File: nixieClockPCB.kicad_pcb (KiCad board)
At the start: 2 copper layers, 51 x 30.3 mm, 23 parts, among them M1 1364_HV, U1 74141, U10 WeMos_D1_mini, U2 74141, U3 74141, U4 74141, U5 74141, U6 74141, U7 74AHC595, U8 74AHC595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

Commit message: layout moving.
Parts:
- removed the M1 at (42.0, 90.5)
- added M2: Nch8200hv, Nixie_footprint_lib:Nch8200hv, B.Cu at (189.2, 27.4)
- M1: renamed from U10; moved to B.Cu
- U1, U2, U3, U4, U5, U6: footprint Package_DIP:DIP-16_W7.62mm_LongPads -> Package_DIP:DIP-16_W7.62mm
- U7, U8, U9: footprint Package_DIP:DIP-16_W7.62mm_LongPads -> nixiemisc:nixiemisc-SOIC16-5.3MM; moved to B.Cu
- moved R1 115.9 mm to (18.6, 32.6), turned to -90 degrees
- moved M1 109.1 mm to (149.1, 65.4), turned to 180 degrees
- moved U6 106.7 mm to (161.8, 19.5), turned to -90 degrees
- moved N1 101.5 mm to (27.4, 32.8), turned to 180 degrees
- moved N6 83.4 mm to (152.9, 32.8), turned to 180 degrees
- moved R2 78.5 mm to (40.1, 32.6), turned to -90 degrees
- moved N2 76.7 mm to (48.9, 32.8), turned to 180 degrees
- moved U5 74.6 mm to (139.6, 19.5), turned to -90 degrees
- moved U1 70.4 mm to (36.3, 19.5), turned to -90 degrees
- moved N3 60.8 mm to (78.9, 32.8), turned to 180 degrees
- moved R5 57.3 mm to (121.9, 32.6), turned to -90 degrees
- moved N5 52.3 mm to (130.7, 32.8), turned to 180 degrees
- moved R3 48.1 mm to (70.1, 32.6), turned to -90 degrees
- moved U2 47.6 mm to (57.8, 19.5), turned to -90 degrees
- moved N4 40.6 mm to (101.9, 32.8), turned to 180 degrees
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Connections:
- U1 pad 3: unconnected-(U1-Pad3) -> N1_A
- U1 pad 4: unconnected-(U1-Pad4) -> N1_D
- U1 pad 6: unconnected-(U1-Pad6) -> N1_B
- U1 pad 7: unconnected-(U1-Pad7) -> N1_C
- U2 pad 3: unconnected-(U2-Pad3) -> N2_A
- U2 pad 4: unconnected-(U2-Pad4) -> N2_D
- U2 pad 6: unconnected-(U2-Pad6) -> N2_B
- U2 pad 7: unconnected-(U2-Pad7) -> N2_C
- U3 pad 3: unconnected-(U3-Pad3) -> N3_A
- U3 pad 4: unconnected-(U3-Pad4) -> N3_D
- U3 pad 6: unconnected-(U3-Pad6) -> N3_B
- U3 pad 7: unconnected-(U3-Pad7) -> N3_C
- U4 pad 3: unconnected-(U4-Pad3) -> N4_A
- U4 pad 4: unconnected-(U4-Pad4) -> N4_D
- U4 pad 6: unconnected-(U4-Pad6) -> N4_B
- U4 pad 7: unconnected-(U4-Pad7) -> N4_C
- U5 pad 3: unconnected-(U5-Pad3) -> N5_A
- U5 pad 4: unconnected-(U5-Pad4) -> N5_D
- U5 pad 6: unconnected-(U5-Pad6) -> N5_B
- U5 pad 7: unconnected-(U5-Pad7) -> N5_C
- U6 pad 3: unconnected-(U6-Pad3) -> N6_A
- U6 pad 4: unconnected-(U6-Pad4) -> N6_D
- U6 pad 6: unconnected-(U6-Pad6) -> N6_B
- U6 pad 7: unconnected-(U6-Pad7) -> N6_C
- U7 pad 1: unconnected-(U7-Pad1) -> N1_B
- U7 pad 15: unconnected-(U7-Pad15) -> N1_A
- U7 pad 2: unconnected-(U7-Pad2) -> N1_C
- U7 pad 3: unconnected-(U7-Pad3) -> N1_D
- U7 pad 4: unconnected-(U7-Pad4) -> N2_A
- U7 pad 5: unconnected-(U7-Pad5) -> N2_B
- U7 pad 6: unconnected-(U7-Pad6) -> N2_C
- U7 pad 7: unconnected-(U7-Pad7) -> N2_D
- U8 pad 1: unconnected-(U8-Pad1) -> N3_B
- U8 pad 15: unconnected-(U8-Pad15) -> N3_A
- U8 pad 2: unconnected-(U8-Pad2) -> N3_C
- U8 pad 3: unconnected-(U8-Pad3) -> N3_D
- U8 pad 4: unconnected-(U8-Pad4) -> N4_A
- U8 pad 5: unconnected-(U8-Pad5) -> N4_B
- U8 pad 6: unconnected-(U8-Pad6) -> N4_C
- U8 pad 7: unconnected-(U8-Pad7) -> N4_D
- U9 pad 1: unconnected-(U9-Pad1) -> N5_B
- U9 pad 15: unconnected-(U9-Pad15) -> N5_A
- U9 pad 2: unconnected-(U9-Pad2) -> N5_C
- U9 pad 3: unconnected-(U9-Pad3) -> N5_D
- U9 pad 4: unconnected-(U9-Pad4) -> N6_A
- U9 pad 5: unconnected-(U9-Pad5) -> N6_B
- U9 pad 6: unconnected-(U9-Pad6) -> N6_C
- U9 pad 7: unconnected-(U9-Pad7) -> N6_D
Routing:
- net Vdrive: track 0.00 -> 126.6 mm
- net N6_A: track 0.00 -> 59.6 mm
- net N6_D: track 0.00 -> 51.8 mm
- net N6_B: track 0.00 -> 51.8 mm, vias 0 -> 1
- net N6_C: track 0.00 -> 47.1 mm, vias 0 -> 1
- net N5_A: track 0.00 -> 43.0 mm
- net Net-(N4-Pad4): track 0.00 -> 31.7 mm
- net Net-(N1-Pad4): track 0.00 -> 31.3 mm
- net Net-(N3-Pad4): track 0.00 -> 31.3 mm
- net Net-(N2-Pad4): track 0.00 -> 31.2 mm
- net N5_D: track 0.00 -> 30.9 mm, vias 0 -> 1
- net Net-(N6-Pad4): track 0.00 -> 30.4 mm, vias 0 -> 2
- net Net-(N5-Pad4): track 0.00 -> 30.1 mm
- net Net-(N1-Pad6): track 0.00 -> 28.9 mm
- net Net-(N3-Pad6): track 0.00 -> 28.9 mm
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- added copper zone on F.Cu, net +5V
- added copper zone on B.Cu, net GND
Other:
- board size 51 x 30.3 mm -> 153 x 29 mm

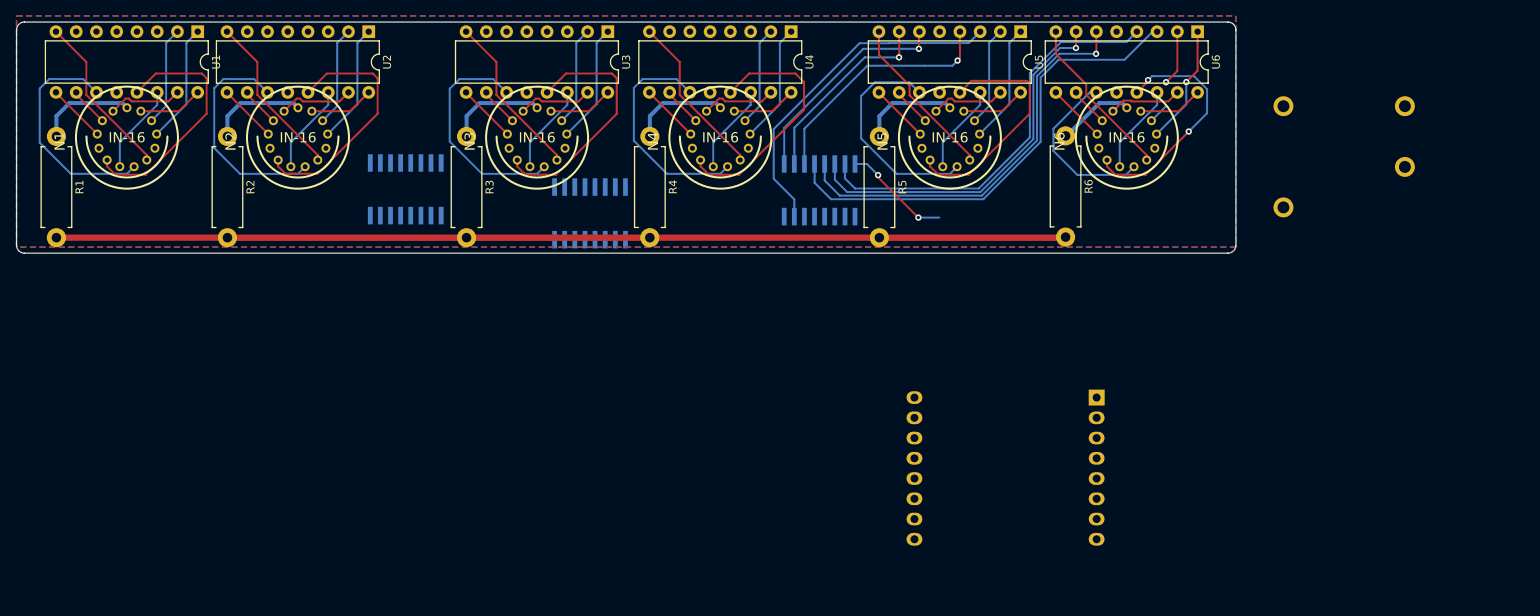
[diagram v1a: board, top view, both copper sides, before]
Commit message: First routing iteration done
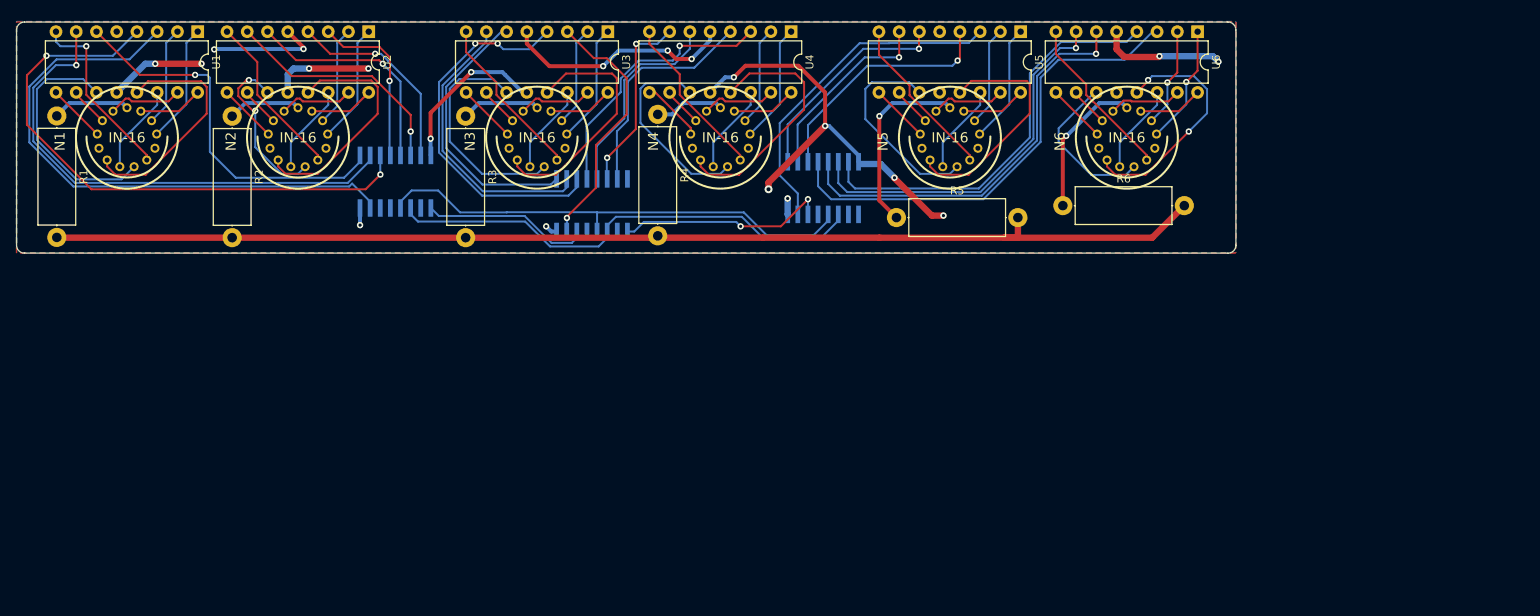
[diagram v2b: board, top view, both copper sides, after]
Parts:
- removed M1: WeMos_D1_mini, Module:WEMOS_D1_mini_light
- removed M2: Nch8200hv, Nixie_footprint_lib:Nch8200hv
- R1, R2, R3, R4, R5, R6: value R -> 20K; footprint Resistor_THT:R_Axial_DIN0411_L9.9mm_D3.6mm_P12.70mm_Horizontal -> Resistor_THT:R_Axial_DIN0414_L11.9mm_D4.5mm_P15.24mm_Horizontal
- moved R5 10.4 mm to (124.0, 42.8), turned to 0 degrees
- moved R6 8.76 mm to (144.9, 41.3), turned to 0 degrees
- moved R4 2.94 mm to (94.0, 29.9)
- moved R2 2.61 mm to (40.6, 30.1)
- moved R1 2.57 mm to (18.6, 30.1)
- moved R3 2.55 mm to (70.0, 30.1)
- moved U7 1.60 mm to (61.1, 38.3)
- moved U8 1.06 mm to (85.8, 41.2)
- moved U9 0.52 mm to (114.8, 39.1)
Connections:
- U7 pad 11: unconnected-(U7-Pad11) -> CLOCK
- U7 pad 12: unconnected-(U7-Pad12) -> LATCH
- U7 pad 14: unconnected-(U7-Pad14) -> DATA
- U7 pad 16: unconnected-(U7-Pad16) -> +5V
- U7 pad 9: unconnected-(U7-Pad9) -> Net-(U8-Pad14)
- U8 pad 11: unconnected-(U8-Pad11) -> CLOCK
- U8 pad 12: unconnected-(U8-Pad12) -> LATCH
- U8 pad 14: unconnected-(U8-Pad14) -> Net-(U8-Pad14)
- U8 pad 16: unconnected-(U8-Pad16) -> +5V
- U8 pad 9: unconnected-(U8-Pad9) -> Net-(U8-Pad9)
- U9 pad 11: unconnected-(U9-Pad11) -> CLOCK
- U9 pad 12: unconnected-(U9-Pad12) -> LATCH
- U9 pad 14: unconnected-(U9-Pad14) -> Net-(U8-Pad9)
- U9 pad 16: unconnected-(U9-Pad16) -> +5V
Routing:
- net GND: track 13.5 -> 97.7 mm, vias 2 -> 11
- net N1_D: track 0.00 -> 73.2 mm, vias 0 -> 2
- net N1_A: track 0.00 -> 72.8 mm
- net +5V: track 0.00 -> 64.6 mm, vias 0 -> 10
- net N1_C: track 0.00 -> 63.7 mm, vias 0 -> 1
- net CLOCK: track 0.00 -> 61.4 mm
- net LATCH: track 0.00 -> 61.3 mm
- net N1_B: track 0.00 -> 47.7 mm, vias 0 -> 1
- net N3_D: track 0.00 -> 46.8 mm, vias 0 -> 2
- net N3_C: track 0.00 -> 36.2 mm
- net N3_B: track 0.00 -> 34.2 mm
- net N4_A: track 0.00 -> 33.7 mm, vias 0 -> 1
- net N3_A: track 0.00 -> 32.3 mm, vias 0 -> 1
- net N2_C: track 0.00 -> 29.9 mm, vias 0 -> 1
- net N2_B: track 0.00 -> 28.6 mm, vias 0 -> 1
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
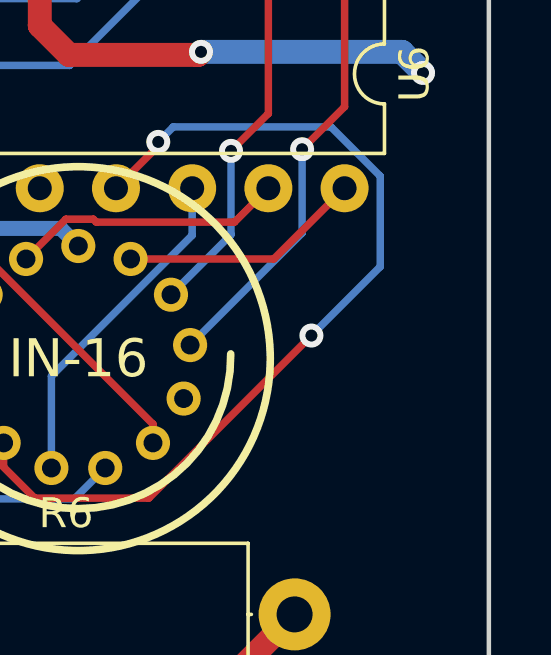
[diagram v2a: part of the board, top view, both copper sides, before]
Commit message: Added input
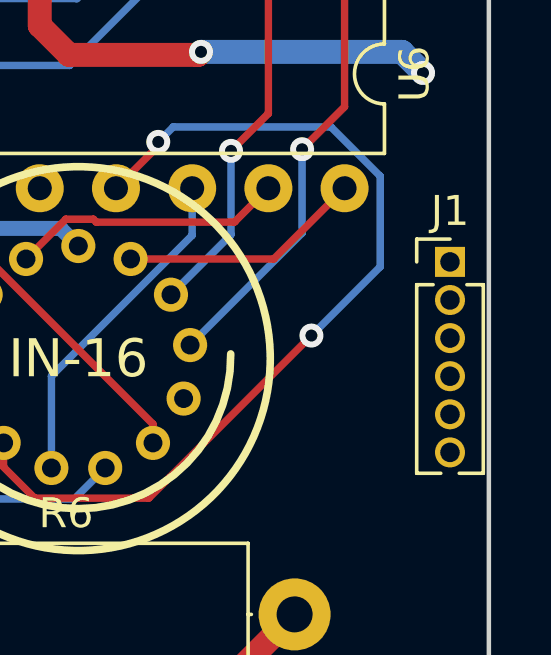
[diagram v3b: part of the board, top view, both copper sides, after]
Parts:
- added J1: Conn_01x06_Female, Connector_PinHeader_1.27mm:PinHeader_1x06_P1.27mm_Vertical, F.Cu at (165.3, 29.6)
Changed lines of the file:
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@@
   (net 115 "unconnected-(U9-Pad13)")
   (net 116 "Net-(U8-Pad9)")
-  (net 117 "Net-(U8-Pad14)")
+  (net 117 "Net-(U7-Pad9)")
   (footprint "Resistor_THT:R_Axial_DIN0414_L11.9mm_D4.5mm_P15.24mm_Horizontal" (layer "F.Cu")
     (at 40.65 30.08 -90)
@@
       (net 1 "Vdrive") (pintype "passive"))
     (model "${KICAD6_3DMODEL_DIR}/Resistor_THT.3dshapes/R_Axial_DIN0414_L11.9mm_D4.5mm_P15.24mm_Horizontal.wrl"
+      (offset (xyz 0 0 0))
+      (scale (xyz 1 1 1))
+      (rotate (xyz 0 0 0))
+    )
+  )
+  (footprint "Connector_PinHeader_1.27mm:PinHeader_1x06_P1.27mm_Vertical" (layer "F.Cu")
+    (at 165.3 29.55)
+    (descr "Through hole straight pin header, 1x06, 1.27mm pitch, single row")
+    (tags "Through hole pin header THT 1x06 1.27mm single row")
+    (property "Sheetfile" "nixieClockPCB.kicad_sch")
+    (property "Sheetname" "")
+    (attr through_hole)
+    (fp_text reference "J1" (at 0 -1.695) (layer "F.SilkS")
+      (effects (font (size 1 1) (thickness 0.15)))
+    )
+    (fp_text value "Conn_01x06_Female" (at 0 8.045) (layer "F.Fab")
+      (effects (font (size 1 1) (thickness 0.15)))
+    )
+    (fp_text user "${REFERENCE}" (at 0 3.175 90) (layer "F.Fab")
+      (effects (font (size 1 1) (thickness 0.15)))
+    )
+    (fp_line (start -1.11 -0.76) (end 0 -0.76) (layer "F.SilkS") (width 0.12))
+    (fp_line (start -1.11 7.045) (end -0.30753 7.045) (layer "F.SilkS") (width 0.12))
+    (fp_line (start -1.11 0) (end -1.11 -0.76) (layer "F.SilkS") (width 0.12))
+    (fp_line (start 0.30753 7.045) (end 1.11 7.045) (layer "F.SilkS") (width 0.12))
+    (fp_line (start 0.563471 0.76) (end 1.11 0.76) (layer "F.SilkS") (width 0.12))
+    (fp_line (start -1.11 0.76) (end -0.563471 0.76) (layer "F.SilkS") (width 0.12))
+    (fp_line (start 1.11 0.76) (end 1.11 7.045) (layer "F.SilkS") (width 0.12))
+    (fp_line (start -1.11 0.76) (end -1.11 7.045) (layer "F.SilkS") (width 0.12))
+    (fp_line (start -1.55 7.5) (end 1.55 7.5) (layer "F.CrtYd") (width 0.05))
+    (fp_line (start 1.55 -1.15) (end -1.55 -1.15) (layer "F.CrtYd") (width 0.05))
+    (fp_line (start -1.55 -1.15) (end -1.55 7.5) (layer "F.CrtYd") (width 0.05))
+    (fp_line (start 1.55 7.5) (end 1.55 -1.15) (layer "F.CrtYd") (width 0.05))
+    (fp_line (start -0.525 -0.635) (end 1.05 -0.635) (layer "F.Fab") (width 0.1))
+    (fp_line (start -1.05 6.985) (end -1.05 -0.11) (layer "F.Fab") (width 0.1))
+    (fp_line (start 1.05 -0.635) (end 1.05 6.985) (layer "F.Fab") (width 0.1))
+    (fp_line (start -1.05 -0.11) (end -0.525 -0.635) (layer "F.Fab") (width 0.1))
+    (fp_line (start 1.05 6.985) (end -1.05 6.985) (layer "F.Fab") (width 0.1))
+    (pad "1" thru_hole rect (at 0 0) (size 1 1) (drill 0.65) (layers *.Cu *.Mask)
+      (net 2 "CLOCK") (pinfunction "Pin_1") (pintype "passive"))
+    (pad "2" thru_hole oval (at 0 1.27) (size 1 1) (drill 0.65) (layers *.Cu *.Mask)
+      (net 108 "DATA") (pinfunction "Pin_2") (pintype "passive"))
+    (pad "3" thru_hole oval (at 0 2.54) (size 1 1) (drill 0.65) (layers *.Cu *.Mask)
+      (net 5 "LATCH") (pinfunction "Pin_3") (pintype "passive"))
+    (pad "4" thru_hole oval (at 0 3.81) (size 1 1) (drill 0.65) (layers *.Cu *.Mask)
+      (net 1 "Vdrive") (pinfunction "Pin_4") (pintype "passive"))
+    (pad "5" thru_hole oval (at 0 5.08) (size 1 1) (drill 0.65) (layers *.Cu *.Mask)
+      (net 4 "+5V") (pinfunction "Pin_5") (pintype "passive"))
+    (pad "6" thru_hole oval (at 0 6.35) (size 1 1) (drill 0.65) (layers *.Cu *.Mask)
+      (net 3 "GND") (pinfunction "Pin_6") (pintype "passive"))
+    (model "${KICAD6_3DMODEL_DIR}/Connector_PinHeader_1.27mm.3dshapes/PinHeader_1x06_P1.27mm_Vertical.wrl"
       (offset (xyz 0 0 0))
       (scale (xyz 1 1 1))
@@
       (net 112 "unconnected-(U8-Pad13)") (pinfunction "~{OE}") (pintype "input"))
     (pad "14" smd rect (at 3.29946 1.905) (size 0.59944 2.19964) (layers "B.Cu" "B.Paste" "B.Mask")
-      (net 117 "Net-(U8-Pad14)") (pinfunction "SER") (pintype "input"))
+      (net 117 "Net-(U7-Pad9)") (pinfunction "SER") (pintype "input"))
     (pad "15" smd rect (at 3.29946 3.175) (size 0.59944 2.19964) (layers "B.Cu" "B.Paste" "B.Mask")
       (net 95 "N3_A") (pinfunction "QA") (pintype "tri_state"))
@@
       (net 3 "GND") (pinfunction "GND") (pintype "power_in"))
     (pad "9" smd rect (at 3.29946 -4.445) (size 0.59944 2.19964) (layers "B.Cu" "B.Paste" "B.Mask")
-      (net 117 "Net-(U8-Pad14)") (pinfunction "QH'") (pintype "output"))
+      (net 117 "Net-(U7-Pad9)") (pinfunction "QH'") (pintype "output"))
     (pad "10" smd rect (at 3.29946 -3.175) (size 0.59944 2.19964) (layers "B.Cu" "B.Paste" "B.Mask")
       (net 109 "unconnected-(U7-Pad10)") (pinfunction "~{SRCLR}") (pintype "input"))

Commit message: added input jumper
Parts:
- moved J1 119.4 mm to (46.6, 42.4), turned to 90 degrees
- moved U7 1.20 mm to (61.1, 37.1)
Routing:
- net CLOCK: track 61.4 -> 82.8 mm, vias 0 -> 1
- net LATCH: track 61.3 -> 79.0 mm, vias 0 -> 1
- net DATA: track 0.00 -> 15.3 mm
- net Vdrive: track 147.4 -> 150.3 mm
- net N1_C: track 63.7 -> 64.9 mm
- net N1_B: track 47.7 -> 48.9 mm
- net N2_D: track 25.1 -> 23.9 mm
- net N2_B: track 28.6 -> 27.4 mm
- net N2_A: track 21.4 -> 20.2 mm
- net GND: track 97.7 -> 96.5 mm
- net N2_C: track 29.9 -> 28.7 mm
- net N1_A: track 72.8 -> 72.2 mm
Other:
- board text added: "5V"
- board text added: "CLK"
- board text added: "DATA"
- board text added: "GND"
- board text added: "HV"
- board text added: "LAT"

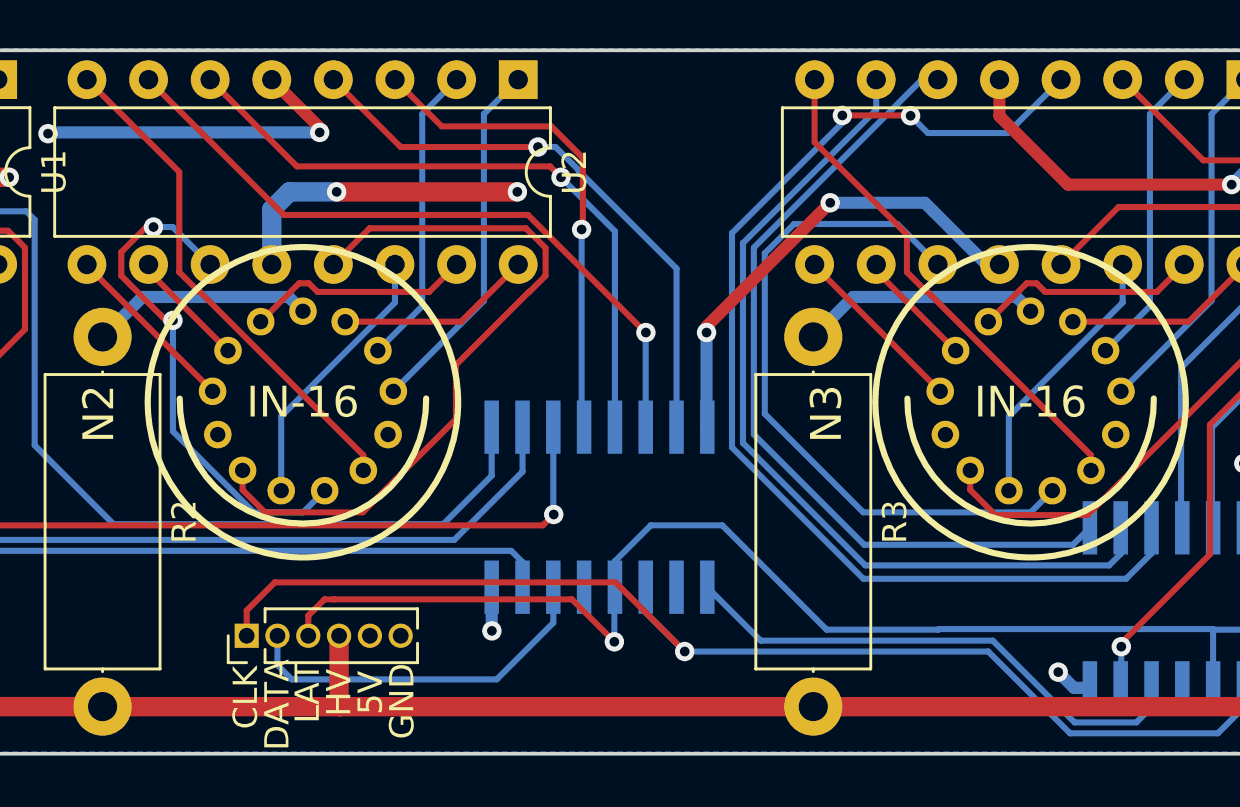
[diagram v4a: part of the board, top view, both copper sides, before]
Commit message: More routing, and gerber generation
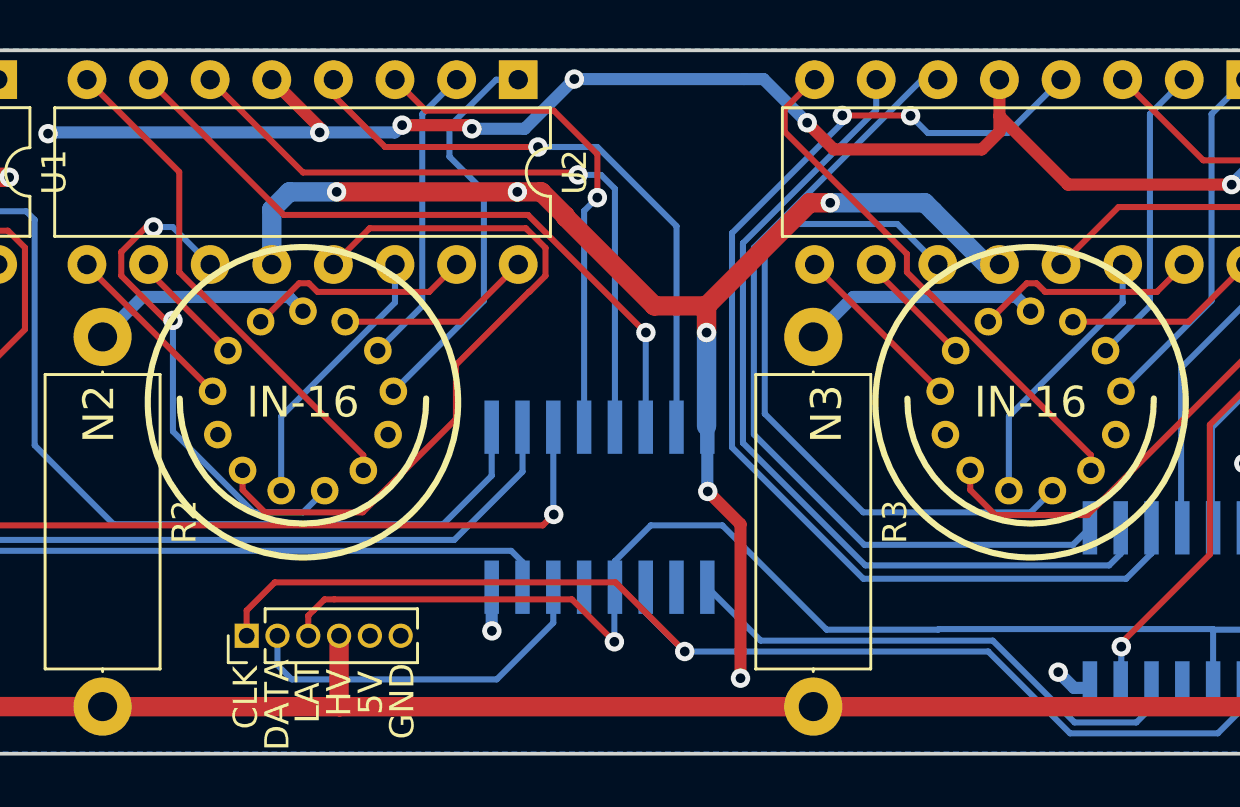
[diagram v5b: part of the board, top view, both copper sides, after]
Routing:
- net +5V: track 64.3 -> 95.5 mm, vias 10 -> 14
- net GND: track 96.5 -> 117.7 mm, vias 11 -> 13
- net Net-(N2-Pad8): track 15.0 -> 16.7 mm
- net N2_D: track 23.9 -> 25.3 mm
- net Net-(N3-Pad2): track 20.9 -> 21.9 mm
- net N2_B: track 27.4 -> 28.4 mm
- net N2_A: track 20.2 -> 21.1 mm
